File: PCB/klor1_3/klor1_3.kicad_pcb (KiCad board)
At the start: 2 copper layers, 160 x 118.2 mm, 89 parts, among them J1 MJ-4PP-9, J2 Haptic Buzz, J3 lv27, SW1 SW_PUSH-MX_W_LED, SW10 SW_PUSH-MX_W_LED, SW11 SW_PUSH-MX_W_LED, SW12 SW_PUSH-MX_W_LED, SW13 SW_PUSH-MX_W_LED, SW14 SW_PUSH-MX_W_LED, SW15 SW_PUSH-MX_W_LED, SW16 SW_PUSH-MX_W_LED, SW17 SW_PUSH-MX_W_LED, SW18 RotaryEncoder_Switch, SW19 SW_PUSH-MX_W_LED, SW2 SW_PUSH-MX_W_LED, SW20 SW_PUSH-MX_W_LED, SW21 SW_PUSH-MX_W_LED, SW22 SW_PUSH-MX_W_LED, SW3 SW_PUSH-MX_W_LED, SW4 SW_PUSH-MX_W_LED, SW5 SW_PUSH-MX_W_LED, SW6 SW_PUSH-MX_W_LED, SW7 SW_PUSH-MX_W_LED, SW8 SW_PUSH-MX_W_LED, SW9 SW_PUSH-MX_W_LED, U1 ProMicro

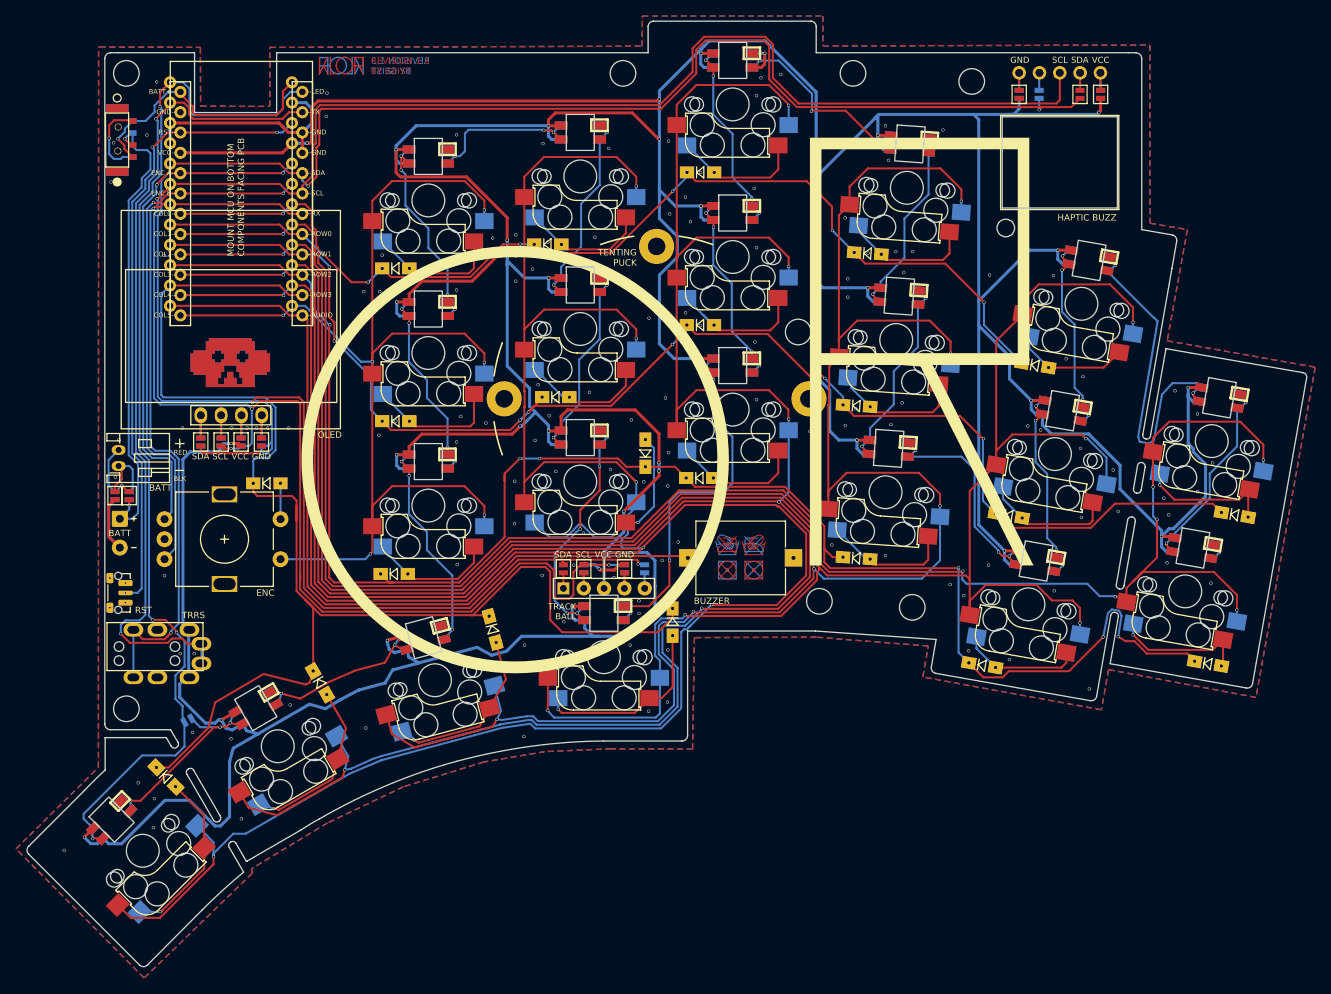
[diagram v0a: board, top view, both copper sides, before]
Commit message: add 5way switch to pcb TODO wires
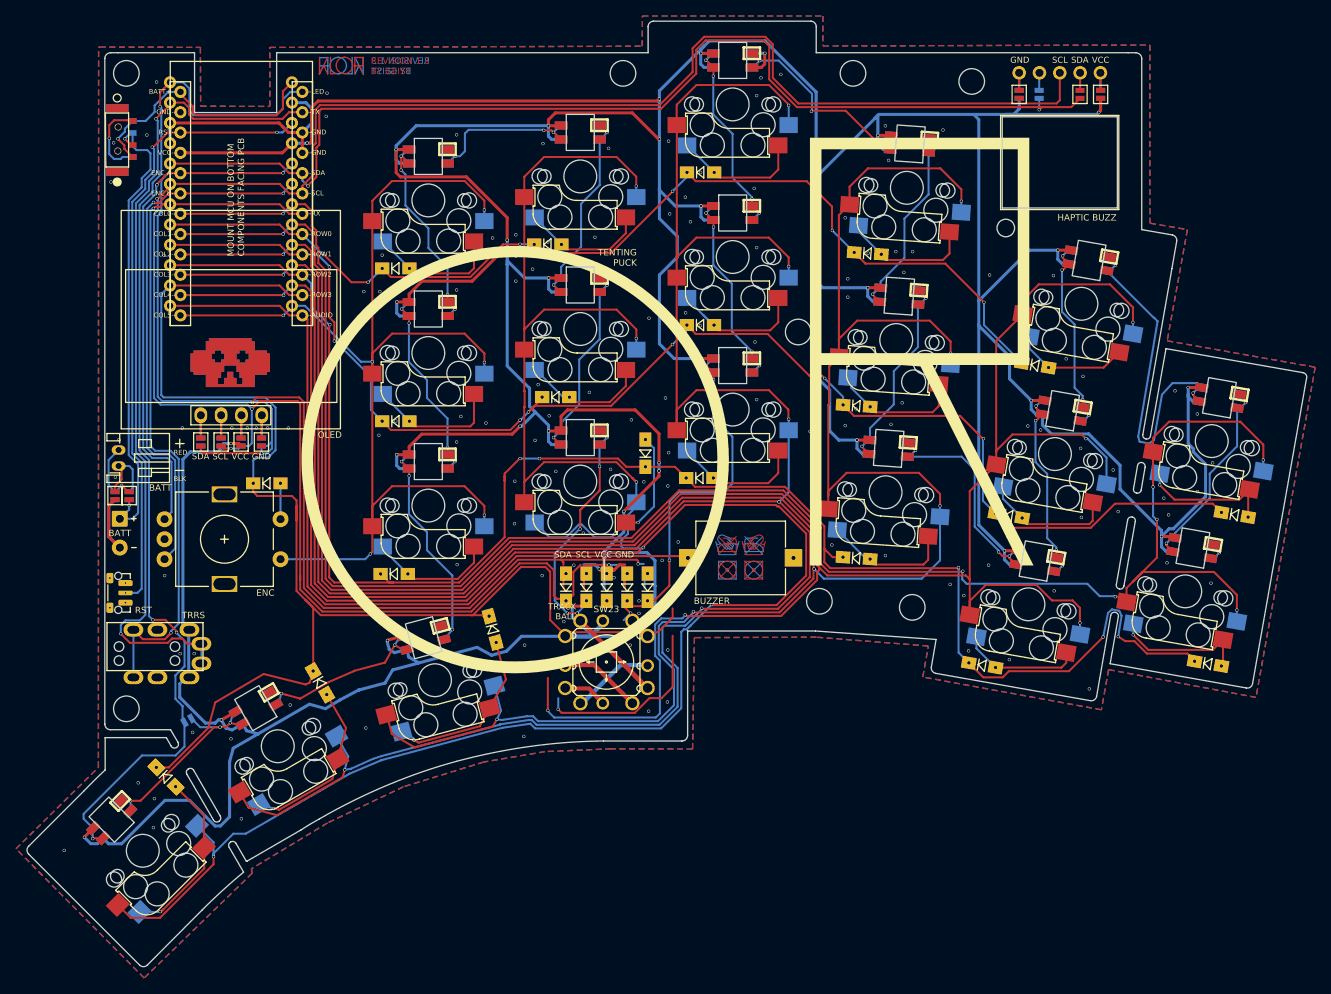
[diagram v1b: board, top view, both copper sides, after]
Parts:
- removed D22: D_Small, KLOR:Diode_SOD123
- removed J3: lv27, KLOR:lvc27_onlyInput
- removed JP16, JP17, JP18, JP19, JP20, JP21: Device_Jumper_NO_Small, KLOR:Jumper
- removed REF**: Tenting Puck, KLOR:SplitkbTentingPuckWithoutCenterHole
- removed SW22: SW_PUSH-MX_W_LED, KLOR:SK6812MINI_and_cherry
- added D23: D_Small, KLOR:Diode_SOD123, F.Cu at (138.3, 120.0)
- added D24: D_Small, KLOR:Diode_SOD123, F.Cu at (140.8, 120.0)
- added D25: D_Small, KLOR:Diode_SOD123, F.Cu at (143.4, 120.0)
- added D26: D_Small, KLOR:Diode_SOD123, F.Cu at (145.9, 120.0)
- added D27: D_Small, KLOR:Diode_SOD123, F.Cu at (148.5, 120.0)
- added SW23: 5Way-Tactile_K1-1506DN-01, reversible-kicad-footprints:5Way-K1-1506DN-01, F.Cu at (143.3, 129.3)
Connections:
- net col5 renamed SW18A
- SW13 pad 1: Net-(SW13-Pad1) -> Net-(SW13B-DOUT)
- SW14 pad 3: Net-(SW14-Pad3) -> Net-(SW13B-DOUT)
- U1 pad 12: AUDIO -> row4
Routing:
- net Net-(SW13B-DOUT): track 0.00 -> 77.1 mm, vias 0 -> 9
- net Net-(SW14-Pad3): track 46.0 -> 0.00 mm, vias 4 -> 0
- net (no net): track 0.00 -> 42.2 mm, vias 0 -> 3
- net Net-(SW13-Pad1): track 31.2 -> 0.00 mm, vias 5 -> 0
- net Net-(D22-Pad2): track 23.7 -> 0.00 mm, vias 1 -> 0
- net unconnected-(PSW1A-A-Pad1): track 10.3 -> 0.00 mm, vias 1 -> 0
- net Net-(J3-Pad2): track 3.88 -> 0.00 mm
- net col2: track 333.2 -> 337.1 mm
- net Net-(J3-Pad4): track 3.84 -> 0.00 mm
- net unconnected-(SW17B-DOUT-Pad1): track 2.34 -> 0.00 mm, vias 1 -> 0
- net SW18A: track 143.9 -> 145.9 mm
- net Net-(J3-Pad1): track 1.95 -> 0.00 mm
- net Net-(J3-Pad5): track 1.94 -> 0.00 mm
